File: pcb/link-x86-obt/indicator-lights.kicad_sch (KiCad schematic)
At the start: 8 parts, among them IC17 IS31FL3218-GRLS2

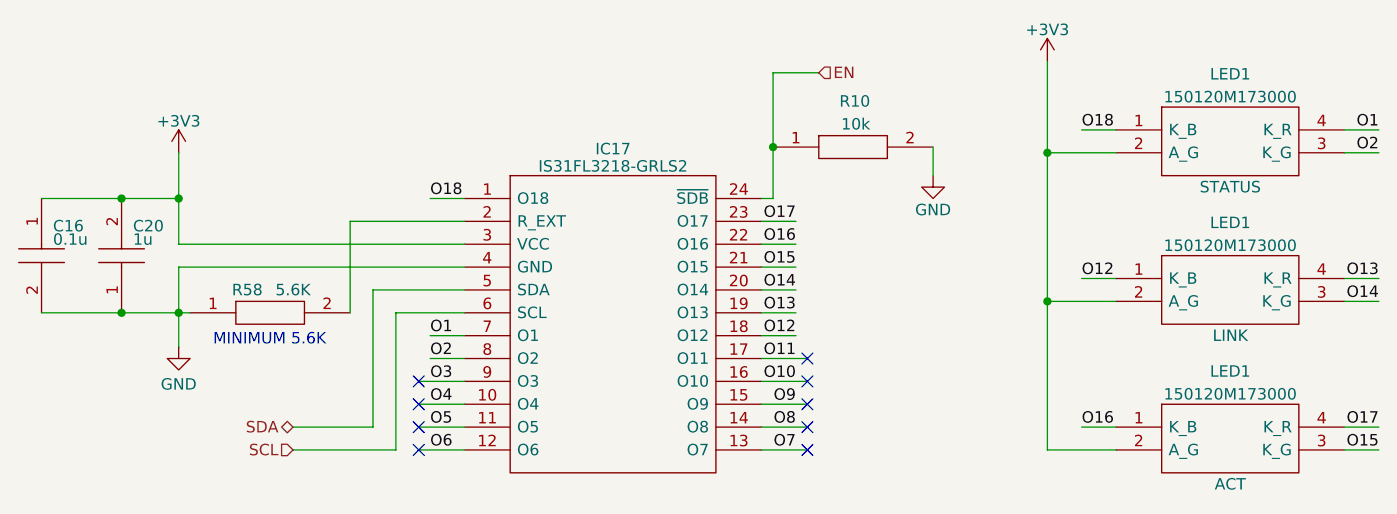
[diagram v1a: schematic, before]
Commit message: increase current limiting resistor for indicator lights
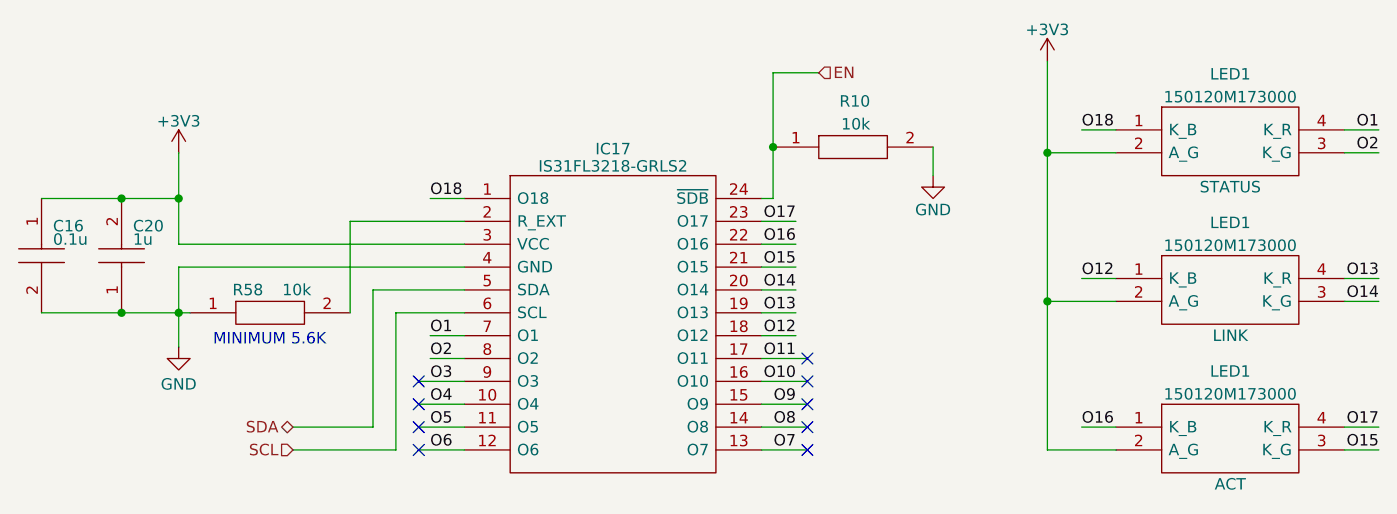
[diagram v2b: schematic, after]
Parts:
- removed R58: 5.6K, RESC1105X40N, symbol Oro:CRGP0402F5K6
- added R58: 10k, RESC1005X40N, symbol SamacSys_Parts:RK73H1ETTP1002F
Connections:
- net GND: now also R58.1
- net at IC17.2 (R_EXT): now also R58.2
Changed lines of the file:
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@@
+	)
+	(symbol
+		(lib_id "SamacSys_Parts:RK73H1ETTP1002F")
+		(at 88.9 109.22 0)
+		(unit 1)
+		(exclude_from_sim no)
+		(in_bom yes)
+		(on_board yes)
+		(dnp no)
+		(property "Reference" "R58"
+			(at 97.028 106.68 0)
+			(effects
+				(font
+					(size 1.27 1.27)
+				)
+				(justify right)
+			)
+		)
+		(property "Value" "10k"
+			(at 102.362 106.68 0)
+			(effects
+				(font
+					(size 1.27 1.27)
+				)
+				(justify right)
+			)
+		)
+		(property "Footprint" "RESC1005X40N"
+			(at 102.87 107.95 0)
+			(effects
+				(font
+					(size 1.27 1.27)
+				)
+				(justify left)
+				(hide yes)
+			)
+		)
+		(property "Datasheet" "http://www.koaspeer.com/catimages/Products/RK73-RT/RK73-RT.pdf"
+			(at 102.87 110.49 0)
+			(effects
+				(font
+					(size 1.27 1.27)
+				)
+				(justify left)
+				(hide yes)
+			)
+		)
+		(property "Description" "Resistor,ThickFilm1005,0.063W,10kohm"
+			(at 102.87 113.03 0)
+			(effects
+				(font
+					(size 1.27 1.27)
+				)
+				(justify left)
+				(hide yes)
+			)
+		)
+		(property "Height" "0.4"
+			(at 102.87 115.57 0)
+			(effects
+				(font
+					(size 1.27 1.27)
+				)
+				(justify left)
+				(hide yes)
+			)
+		)
+		(property "Manufacturer_Name" "KOA Speer"
+			(at 102.87 118.11 0)
+			(effects
+				(font
+					(size 1.27 1.27)
+				)
+				(justify left)
+				(hide yes)
+			)
+		)
+		(property "Manufacturer_Part_Number" "RK73H1ETTP1002F"
+			(at 102.87 120.65 0)
+			(effects
+				(font
+					(size 1.27 1.27)
+				)
+				(justify left)
+				(hide yes)
+			)
+		)
+		(property "Mouser Part Number" "660-RK73H1ETTP1002F"
+			(at 102.87 123.19 0)
+			(effects
+				(font
+					(size 1.27 1.27)
+				)
+				(justify left)
+				(hide yes)
+			)
+		)
+		(property "Mouser Price/Stock" "https://www.mouser.co.uk/ProductDetail/KOA-Speer/RK73H1ETTP1002F?qs=uLfVlVfCHH2OZ4JTybrBPQ%3D%3D"
+			(at 102.87 125.73 0)
+			(effects
+				(font
+					(size 1.27 1.27)
+				)
+				(justify left)
+				(hide yes)
+			)
+		)
+		(property "Arrow Part Number" "RK73H1ETTP1002F"
+			(at 102.87 128.27 0)
+			(effects
+				(font
+					(size 1.27 1.27)
+				)
+				(justify left)
+				(hide yes)
+			)
+		)
+		(property "Arrow Price/Stock" "https://www.arrow.com/en/products/rk73h1ettp1002f/koa-speer-electronics?region=nac"
+			(at 102.87 130.81 0)
+			(effects
+				(font
+					(size 1.27 1.27)
+				)
+				(justify left)
+				(hide yes)
+			)
+		)
+		(property "Mouser Testing Part Number" ""
+			(at 102.87 133.35 0)
+			(effects
+				(font
+					(size 1.27 1.27)
+				)
+				(justify left)
+				(hide yes)
+			)
+		)
+		(property "Mouser Testing Price/Stock" ""
+			(at 102.87 135.89 0)
+			(effects
+				(font
+					(size 1.27 1.27)
+				)
+				(justify left)
+				(hide yes)
+			)
+		)
+		(pin "1"
+		)
+		(pin "2"
+		)
+		(instances
+			(project "OroLink"
+				(path "/e89dcd22-1250-4a5b-b778-1c95a0dd623d/49c51f54-e113-47ff-b1ad-86c9ad73cafa"
+					(reference "R58")
+					(unit 1)
+				)
+			)
+		)
 	)
 	(symbol
@@
 					(unit 1)
 				)
-			)
-		)
-	)
-	(symbol
-		(lib_id "Oro:CRGP0402F5K6")
-		(at 88.9 109.22 0)
-		(unit 1)
-		(exclude_from_sim no)
-		(in_bom yes)
-		(on_board yes)
-		(dnp no)
-		(property "Reference" "R58"
-			(at 95.25 106.68 0)
-			(effects
-				(font
-					(size 1.27 1.27)
-				)
-			)
-		)
-		(property "Value" "5.6K"
-			(at 100.33 106.68 0)
-			(effects
-				(font
-					(size 1.27 1.27)
-				)
-			)
-		)
-		(property "Footprint" "RESC1105X40N"
-			(at 102.87 107.95 0)
-			(effects
-				(font
-					(size 1.27 1.27)
-				)
-				(justify left)
-				(hide yes)
-			)
-		)
-		(property "Datasheet" "https://www.mouser.de/datasheet/2/418/8/ENG_DS_9_1773463_9_B-1358566.pdf"
-			(at 102.87 110.49 0)
-			(effects
-				(font
-					(size 1.27 1.27)
-				)
-				(justify left)
-				(hide yes)
-			)
-		)
-		(property "Description" "5.6k 0402 Thick Film Resistor +/-1% 0.12W CRGP0402F5K6"
-			(at 102.87 113.03 0)
-			(effects
-				(font
-					(size 1.27 1.27)
-				)
-				(justify left)
-				(hide yes)
-			)
-		)
-		(property "Height" "0.4"
-			(at 102.87 115.57 0)
-			(effects
-				(font
-					(size 1.27 1.27)
-				)
-				(justify left)
-				(hide yes)
-			)
-		)
-		(property "Manufacturer_Name" "TE Connectivity"
-			(at 102.87 118.11 0)
-			(effects
-				(font
-					(size 1.27 1.27)
-				)
-				(justify left)
-				(hide yes)
-			)
-		)
-		(property "Manufacturer_Part_Number" "CRGP0402F5K6"
-			(at 102.87 120.65 0)
-			(effects
-				(font
-					(size 1.27 1.27)
-				)
-				(justify left)
-				(hide yes)
-			)
-		)
-		(property "Mouser Part Number" "279-CRGP0402F5K6"
-			(at 102.87 123.19 0)
-			(effects
-				(font
-					(size 1.27 1.27)
-				)
-				(justify left)
-				(hide yes)
-			)
-		)
-		(property "Mouser Price/Stock" "https://www.mouser.de/ProductDetail/TE-Connectivity-Holsworthy/CRGP0402F5K6?qs=wUXugUrL1qxVwNCmbd06hg%3D%3D"
-			(at 102.87 125.73 0)
-			(effects
-				(font
-					(size 1.27 1.27)
-				)
-				(justify left)
-				(hide yes)
-			)
-		)
-		(property "Arrow Part Number" ""
-			(at 102.87 128.27 0)
-			(effects
-				(font
-					(size 1.27 1.27)
-				)
-				(justify left)
-				(hide yes)
-			)
-		)
-		(property "Arrow Price/Stock" ""
-			(at 102.87 130.81 0)
-			(effects
-				(font
-					(size 1.27 1.27)
-				)
-				(justify left)
-				(hide yes)
-			)
-		)
-		(pin "1"
-		)
-		(pin "2"
-		)
-		(instances
-			(project "OroLink"
-				(path "/e89dcd22-1250-4a5b-b778-1c95a0dd623d/49c51f54-e113-47ff-b1ad-86c9ad73cafa"
-					(reference "R58")
-					(unit 1)
-				)
